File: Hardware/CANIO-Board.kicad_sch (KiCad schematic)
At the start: 0 parts

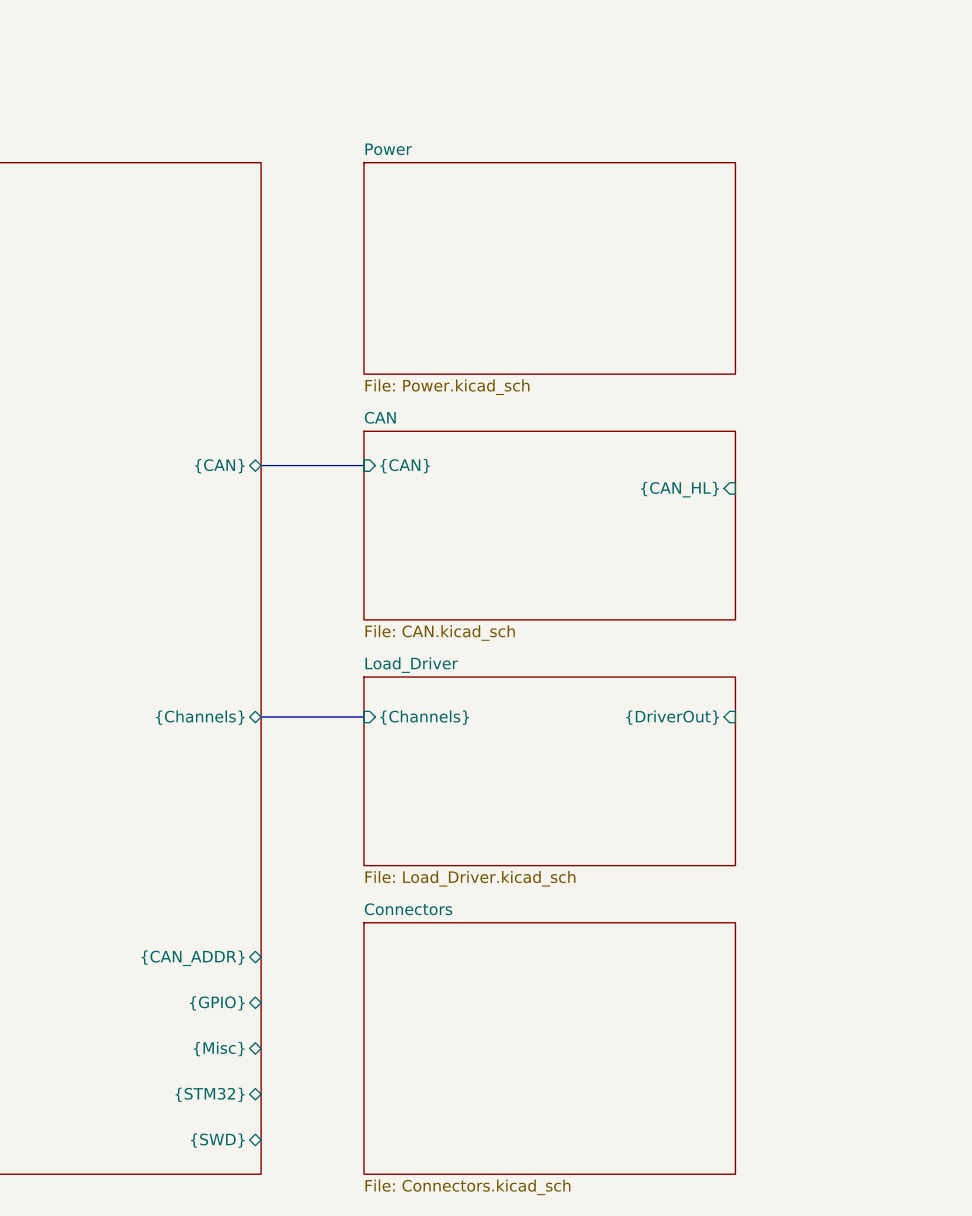
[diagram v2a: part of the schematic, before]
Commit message: Finished final touches on schematic.
- Schematic is complete (NOT yet checked by Yassa/Val)
- ERC check is complete, understandable errors excused w/ comments
- Final schematic formatting complete

Co-authored-by: Kostadin Madjovski <155325994+bivein@users.noreply.github.com>
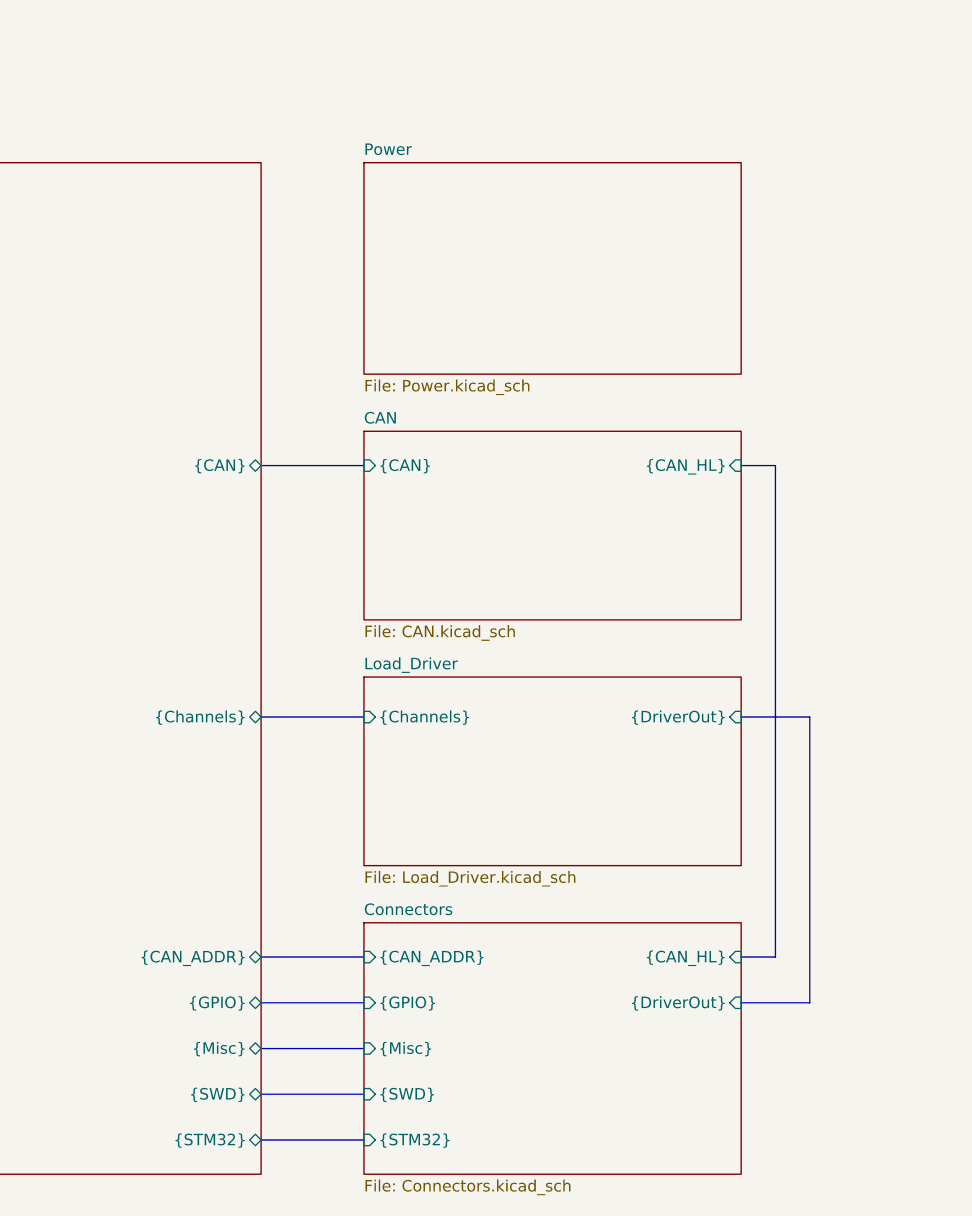
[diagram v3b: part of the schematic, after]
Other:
- sheet Connectors ports: added {CAN_ADDR}, {CAN_HL}, {DriverOut}, {GPIO}, {Misc}, {STM32}, {SWD}; removed none
- company: (none) -> NJIT Solar Car
- title: (none) -> CAN IO Board
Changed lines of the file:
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@@
 	(generator_version "9.0")
 	(paper "USLetter")
+	(title_block
+		(title "CAN IO Board")
+		(date "2026-06-09")
+		(rev "A")
+		(company "NJIT Solar Car")
+		(comment 1 "Author(s): Kostadin Madjovski, Arnav Revankar")
+	)
+	(bus_alias "CAN_HL"
+		(members "CANH_+" "CANL_-")
+	)
 	(text "CAN IO Board for NJIT Solar Car"
 		(exclude_from_sim no)
@@
 	(bus
 		(pts
+			(xy 93.98 167.64) (xy 105.41 167.64)
+		)
+		(stroke
+			(width 0)
+			(type default)
+		)
+	)
+	(bus
+		(pts
+			(xy 147.32 125.73) (xy 154.94 125.73)
+		)
+		(stroke
+			(width 0)
+			(type default)
+		)
+	)
+	(bus
+		(pts
+			(xy 147.32 97.79) (xy 151.13 97.79)
+		)
+		(stroke
+			(width 0)
+			(type default)
+		)
+	)
+	(bus
+		(pts
+			(xy 93.98 125.73) (xy 105.41 125.73)
+		)
+		(stroke
+			(width 0)
+			(type default)
+		)
+	)
+	(bus
+		(pts
+			(xy 93.98 157.48) (xy 105.41 157.48)
+		)
+		(stroke
+			(width 0)
+			(type default)
+		)
+	)
+	(bus
+		(pts
+			(xy 93.98 162.56) (xy 105.41 162.56)
+		)
+		(stroke
+			(width 0)
+			(type default)
+		)
+	)
+	(bus
+		(pts
 			(xy 93.98 97.79) (xy 105.41 97.79)
 		)
@@
 	(bus
 		(pts
-			(xy 93.98 125.73) (xy 105.41 125.73)
+			(xy 154.94 157.48) (xy 147.32 157.48)
+		)
+		(stroke
+			(width 0)
+			(type default)
+		)
+	)
+	(bus
+		(pts
+			(xy 93.98 152.4) (xy 105.41 152.4)
+		)
+		(stroke
+			(width 0)
+			(type default)
+		)
+	)
+	(bus
+		(pts
+			(xy 154.94 125.73) (xy 154.94 157.48)
+		)
+		(stroke
+			(width 0)
+			(type default)
+		)
+	)
+	(bus
+		(pts
+			(xy 151.13 152.4) (xy 147.32 152.4)
+		)
+		(stroke
+			(width 0)
+			(type default)
+		)
+	)
+	(bus
+		(pts
+			(xy 151.13 97.79) (xy 151.13 152.4)
+		)
+		(stroke
+			(width 0)
+			(type default)
+		)
+	)
+	(bus
+		(pts
+			(xy 93.98 172.72) (xy 105.41 172.72)
 		)
 		(stroke
@@
 	)
 	(image
-		(at 229.87 45.085)
-		(scale 1.4523)
+		(at 224.79 54.61)
+		(scale 2.10587)
 		(data "/9j/4AAQSkZJRgABAQAAAQABAAD/2wBDAAMCAgMCAgMDAwMEAwMEBQgFBQQEBQoHBwYIDAoMDAsK"
 			"CwsNDhIQDQ4RDgsLEBYQERMUFRUVDA8XGBYUGBIUFRT/2wBDAQMEBAUEBQkFBQkUDQsNFBQUFBQU"
@@
 	(sheet
 		(at 105.41 121.285)
-		(size 41.275 20.955)
+		(size 41.91 20.955)
 		(exclude_from_sim no)
 		(in_bom yes)
@@
 		)
 		(pin "{DriverOut}" input
-			(at 146.685 125.73 0)
+			(at 147.32 125.73 0)
 			(effects
 				(font
@@
 		)
 		(pin "{STM32}" bidirectional
+			(at 93.98 172.72 0)
+			(effects
+				(font
+					(size 1.27 1.27)
+				)
+				(justify right)
+			)
+		)
+		(pin "{SWD}" bidirectional
 			(at 93.98 167.64 0)
-			(effects
-				(font
-					(size 1.27 1.27)
-				)
-				(justify right)
-			)
-		)
-		(pin "{SWD}" bidirectional
-			(at 93.98 172.72 0)
 			(effects
 				(font
@@
 	(sheet
 		(at 105.41 64.135)
-		(size 41.275 23.495)
+		(size 41.91 23.495)
 		(exclude_from_sim no)
 		(in_bom yes)
@@
 	(sheet
 		(at 105.41 148.59)
-		(size 41.275 27.94)
+		(size 41.91 27.94)
 		(exclude_from_sim no)
 		(in_bom yes)
@@
 			)
 		)
+		(pin "{CAN_ADDR}" input
+			(at 105.41 152.4 180)
+			(effects
+				(font
+					(size 1.27 1.27)
+				)
+				(justify left)
+			)
+		)
+		(pin "{CAN_HL}" input
+			(at 147.32 152.4 0)
+			(effects
+				(font
+					(size 1.27 1.27)
+				)
+				(justify right)
+			)
+		)
+		(pin "{DriverOut}" input
+			(at 147.32 157.48 0)
+			(effects
+				(font
+					(size 1.27 1.27)
+				)
+				(justify right)
+			)
+		)
+		(pin "{GPIO}" input
+			(at 105.41 157.48 180)
+			(effects
+				(font
+					(size 1.27 1.27)
+				)
+				(justify left)
+			)
+		)
+		(pin "{Misc}" input
+			(at 105.41 162.56 180)
+			(effects
+				(font
+					(size 1.27 1.27)
+				)
+				(justify left)
+			)
+		)
+		(pin "{SWD}" input
+			(at 105.41 167.64 180)
+			(effects
+				(font
+					(size 1.27 1.27)
+				)
+				(justify left)
+			)
+		)
+		(pin "{STM32}" input
+			(at 105.41 172.72 180)
+			(effects
+				(font
+					(size 1.27 1.27)
+				)
+				(justify left)
+			)
+		)
 		(instances
 			(project "CANIO-Board"
@@
 	(sheet
 		(at 105.41 93.98)
-		(size 41.275 20.955)
+		(size 41.91 20.955)
 		(exclude_from_sim no)
 		(in_bom yes)
@@
 		)
 		(pin "{CAN_HL}" input
-			(at 146.685 100.33 0)
-			(effects
-				(font
+			(at 147.32 97.79 0)
+			(effects
+				(font
